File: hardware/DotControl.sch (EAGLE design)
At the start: 48 parts, among them CN1 1X4-BIG, IC1 MCP1703CB, J3 USB-MICROB, SW2 Previous, SW5 Previous, SW6 Next, SW8 Ok, U1 ATMEGA328P-MU-QFN32, U2 TMP102, U3 ATSHA204-TSU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

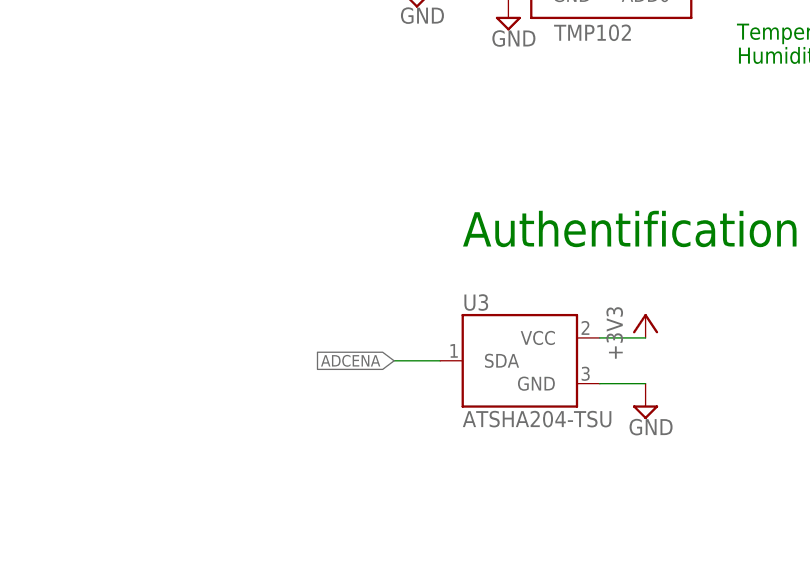
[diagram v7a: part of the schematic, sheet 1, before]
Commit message: Add missing pullup to crypto chip
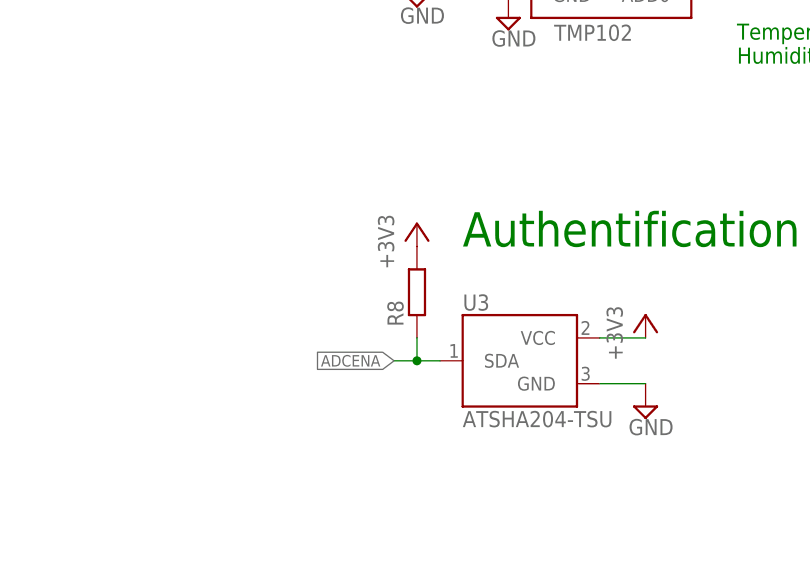
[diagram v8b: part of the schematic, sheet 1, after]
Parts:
- added R8: (no value), rcl:R-EU_R0603
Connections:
- net +3V3: now also R8.2
- net ADCENA: now also R8.1
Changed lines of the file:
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@@
 <part name="C9" library="rcl" deviceset="C-EU" device="C0603" value="1uF"/>
 <part name="SUPPLY26" library="supply2" deviceset="GND" device=""/>
+<part name="R8" library="rcl" deviceset="R-EU_" device="R0603"/>
+<part name="+3V15" library="supply1" deviceset="+3V3" device=""/>
 </parts>
 <sheets>
@@
 <instance part="C9" gate="G$1" x="347.98" y="25.4" rot="R90"/>
 <instance part="SUPPLY26" gate="GND" x="363.22" y="15.24"/>
+<instance part="R8" gate="G$1" x="203.2" y="66.04" rot="R90"/>
+<instance part="+3V15" gate="G$1" x="203.2" y="73.66"/>
 </instances>
 <busses>
@@
 <junction x="505.46" y="228.6"/>
 </segment>
+<segment>
+<pinref part="R8" gate="G$1" pin="2"/>
+<pinref part="+3V15" gate="G$1" pin="+3V3"/>
+</segment>
 </net>
 <net name="PUSH" class="0">
@@
 <segment>
 <pinref part="U3" gate="G$1" pin="SDA"/>
-<wire x1="205.74" y1="58.42" x2="200.66" y2="58.42" width="0.1524" layer="91"/>
+<wire x1="205.74" y1="58.42" x2="203.2" y2="58.42" width="0.1524" layer="91"/>
 <label x="200.66" y="58.42" size="1.27" layer="95" rot="R180" xref="yes"/>
-</segment>
-<segment>
+<pinref part="R8" gate="G$1" pin="1"/>
+<wire x1="203.2" y1="58.42" x2="200.66" y2="58.42" width="0.1524" layer="91"/>
+<wire x1="203.2" y1="60.96" x2="203.2" y2="58.42" width="0.1524" layer="91"/>
+<junction x="203.2" y="58.42"/>
+</segment>
+<segment>
